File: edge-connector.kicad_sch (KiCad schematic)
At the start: 11 parts, among them J1 PCB-Edge_DC-SCM-2.1_2x84_Rev-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, U7 TPS564247DRLR

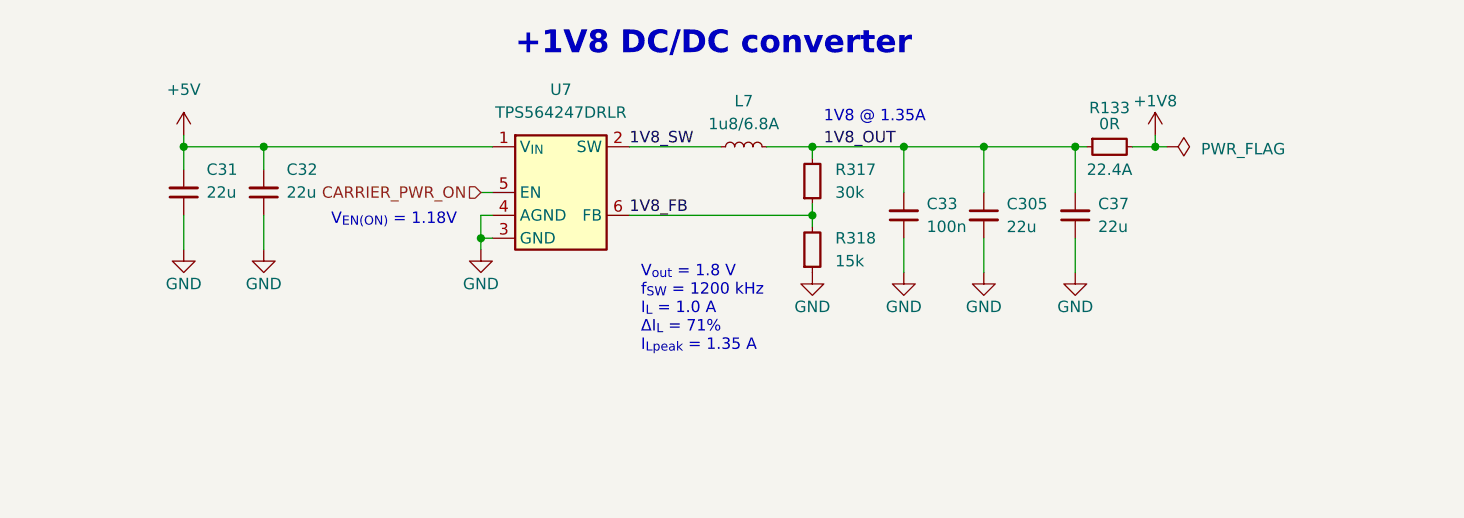
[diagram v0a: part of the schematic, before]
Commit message: [#100720] Swap DCDC for LDO
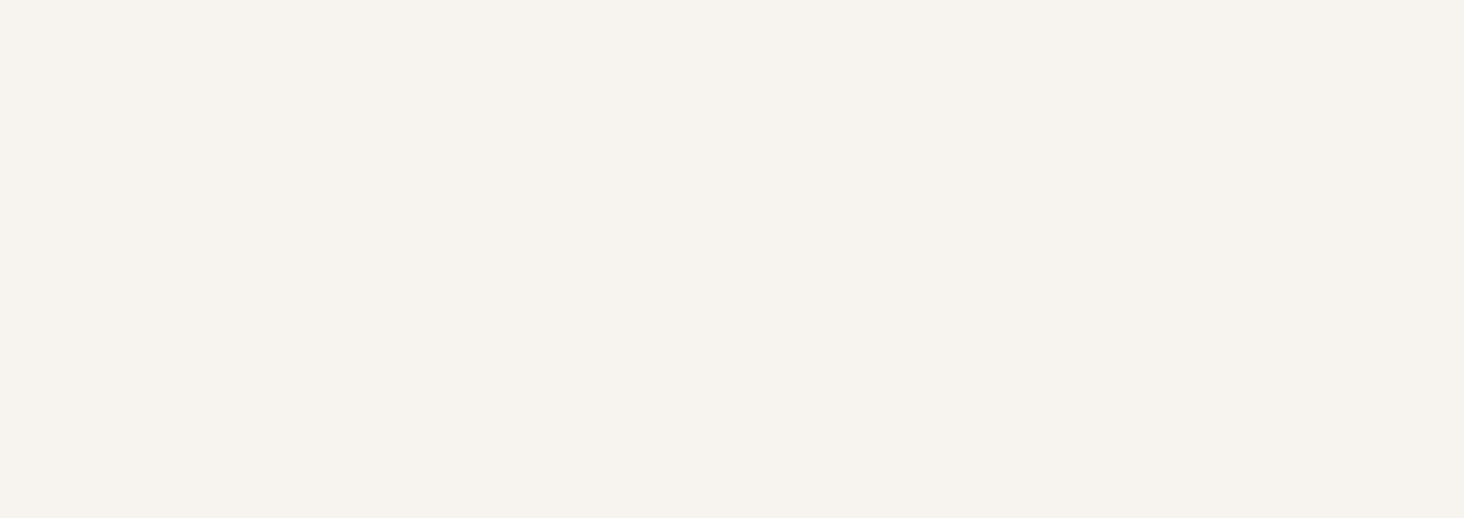
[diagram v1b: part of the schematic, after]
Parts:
- removed C305, C31, C32, C37: C_22u_16V_0603, antmicro-footprints:C_0603_1608Metric_EIA, symbol antmicroCapacitors0603:C_22u_16V_0603
- removed C33: C_100n_0402, antmicro-footprints:C_0402_1005Metric, symbol antmicroCapacitors0402:C_100n_0402
- removed L7: L_1u8_6.8A_WE-MAPI-4020, antmicro-footprints:L_WE-MAPI-4020, symbol antmicroFixedInductors:L_1u8_6.8A_WE-MAPI-4020
- removed R133: R_0R_22.4A_0603, antmicro-footprints:R_0603_1608Metric, symbol antmicroResistors0603:R_0R_22.4A_0603
- removed R317: R_30k_0402, antmicro-footprints:R_0402_1005Metric, symbol antmicroResistors0402:R_30k_0402
- removed R318: R_15k_0402, antmicro-footprints:R_0402_1005Metric, symbol antmicroResistors0402:R_15k_0402
- removed U7: TPS564247DRLR, antmicro-footprints:SOT-563, symbol antmicroDCDCConverters:TPS564247DRLR
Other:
- note removed: "+1V8 DC/DC converter"
- note removed: "1V8 @ 1.35A"
- note removed: "V_{EN(ON)} = 1.18V"
- note removed: "V_{out} = 1.8 V f_{SW} = 1200 kHz I_{L} = 1.0 A ΔI_{L} = 71% I_{Lpeak} = 1.35 A"

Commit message: [#100720] Add DCDC
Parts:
- added C305, C31, C32, C37: C_22u_16V_0603, antmicro-footprints:C_0603_1608Metric_EIA, symbol antmicroCapacitors0603:C_22u_16V_0603
- added C33: C_100n_0402, antmicro-footprints:C_0402_1005Metric, symbol antmicroCapacitors0402:C_100n_0402
- added L7: L_1u8_6.8A_WE-MAPI-4020, antmicro-footprints:L_WE-MAPI-4020, symbol antmicroFixedInductors:L_1u8_6.8A_WE-MAPI-4020
- added R133: R_0R_22.4A_0603, antmicro-footprints:R_0603_1608Metric, symbol antmicroResistors0603:R_0R_22.4A_0603
- added R317: R_30k_0402, antmicro-footprints:R_0402_1005Metric, symbol antmicroResistors0402:R_30k_0402
- added R318: R_15k_0402, antmicro-footprints:R_0402_1005Metric, symbol antmicroResistors0402:R_15k_0402
- added U7: TPS564247DRLR, antmicro-footprints:SOT-563, symbol antmicroDCDCConverters:TPS564247DRLR
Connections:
- net GND: now also C305.2, C31.1, C32.1, C33.1, C37.1, R318.1, U7.3 (GND), U7.4 (AGND)
- new net +1V8: R133.2
- new net +5V: C31.2, C32.2, U7.1 (V_{IN})
- new net 1V8_FB: R317.1, R318.2, U7.6 (FB)
- new net 1V8_OUT: C305.1, C33.2, C37.2, L7.2, R133.1, R317.2
- new net 1V8_SW: L7.1, U7.2 (SW)
- new net CARRIER_PWR_ON: U7.5 (EN)
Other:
- note added: "+1V8 DC/DC converter"
- note added: "1V8 @ 1.35A"
- note added: "V_{EN(ON)} = 1.18V"
- note added: "V_{out} = 1.8 V f_{SW} = 1200 kHz I_{L} = 1.0 A ΔI_{L} = 71% I_{Lpeak} = 1.35 A"
